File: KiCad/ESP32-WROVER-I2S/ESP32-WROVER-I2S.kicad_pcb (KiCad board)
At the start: 2 copper layers, 72 x 47 mm, 31 parts, among them J1 Ext_con, J2 Audio_Con, J3 USB_C_Receptacle_USB2.0_16P, Q1 BSS138, Q2 BSS138, SW1 FLASH, SW2 RESET, U1 ESP32-WROVER, U2 AMS1117-3.3, U3 CH340K

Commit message: ガーバー出力
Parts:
- removed C7: 1u, Capacitor_SMD:C_0603_1608Metric_Pad1.08x0.95mm_HandSolder
- removed C8: 0.1u, Capacitor_SMD:C_0603_1608Metric_Pad1.08x0.95mm_HandSolder
- removed Q1, Q2: BSS138, Package_TO_SOT_SMD:SOT-23
- removed R5, R6: 5.1k, Resistor_SMD:R_0603_1608Metric_Pad0.98x0.95mm_HandSolder
- removed SW1: FLASH, Button_Switch_SMD:SW_Push_SPST_NO_Alps_SKRK
- removed SW2: RESET, Button_Switch_SMD:SW_Push_SPST_NO_Alps_SKRK
- removed U3: CH340K, Package_SO:SSOP-10-1EP_3.9x4.9mm_P1mm_EP2.1x3.3mm
- added D3: D_Schottky, Diode_SMD:D_SOD-123, F.Cu at (157.0, 106.2)
- added J4: Downloader, Connector_PinSocket_2.54mm:PinSocket_1x06_P2.54mm_Vertical, F.Cu at (153.5, 86.4)
- J2: footprint Connector_PinHeader_2.54mm:PinHeader_1x03_P2.54mm_Vertical -> Connector_JST:JST_XH_B3B-XH-A_1x03_P2.50mm_Vertical
- J3: value USB_C_Receptacle_USB2.0_16P -> Power_Con; footprint Connector_USB:USB_C_Receptacle_XKB_U262-16XN-4BVC11 -> Connector_JST:JST_XH_B2B-XH-A_1x02_P2.50mm_Vertical
- moved J3 52.5 mm to (171.5, 111.8), turned to 0 degrees
- moved U2 48.8 mm to (162.6, 110.2), turned to -90 degrees
- moved D1 45.9 mm to (175.8, 107.3)
- moved F1 44.9 mm to (170.8, 107.0), turned to 180 degrees
- moved C1 44.3 mm to (160.6, 104.0), turned to 0 degrees
- moved R1 42.9 mm to (175.8, 105.5)
- moved J1 40.7 mm to (203.3, 74.7)
- moved J2 38.1 mm to (181.7, 90.8), turned to 90 degrees
- moved C2 38.0 mm to (164.4, 104.0), turned to 0 degrees
- moved C6 25.8 mm to (206.0, 109.9)
- moved A1 9.26 mm to (196.2, 98.9), turned to 90 degrees
- moved H2 9.00 mm to (210.0, 73.0)
- moved H4 9.00 mm to (210.0, 114.0)
- moved R3 7.57 mm to (181.5, 96.2), turned to 180 degrees
- moved R2 6.89 mm to (154.2, 82.1)
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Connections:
- C2 pad 1: +3.3V -> Net-(D3-A)
- F1 pad 1: Net-(F1-Pad1) -> Net-(J3-Pin_1)
- U2 pad 2: +3.3V -> Net-(D3-A)
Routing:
- net GND: track 278.0 -> 192.6 mm, vias 5 -> 7
- net +3.3V: track 131.0 -> 183.3 mm, vias 2 -> 1
- net /GPIO34: track 37.0 -> 81.3 mm, vias 1 -> 0
- net /DN: track 40.0 -> 0.00 mm
- net /DP: track 29.0 -> 0.00 mm
- net /GPIO13: track 10.8 -> 37.6 mm
- net /GPIO14: track 17.7 -> 43.2 mm
- net +5V: track 84.5 -> 59.5 mm
- net /EN: track 43.0 -> 18.6 mm, vias 2 -> 0
- net /GPIO12: track 14.5 -> 37.9 mm
- net /DTR: track 22.1 -> 0.00 mm, vias 2 -> 0
- net /GPIO33: track 23.9 -> 42.7 mm
- net /GPIO32: track 26.4 -> 44.2 mm
- net Net-(D3-A): track 0.00 -> 16.7 mm
- net /RTS: track 15.6 -> 0.00 mm, vias 2 -> 0
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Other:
- board size 72 x 47 mm -> 63 x 47 mm
- board text added: "3.3V"
- board text added: "3.3v"
- board text added: "5V GND"
- board text added: "Downloader"
- board text added: "EN"
- board text added: "ESP32-WROVER & I2S REV1 KUNI-NET 2025"
- board text added: "GPIO0"
- board text added: "ROUT GND LOUT"
- board text added: "RxD->TxD"
- board text added: "TxD->RxD"
- board text removed: "ESP32-WROVER & I2S BOARD REV1"
- board text removed: "FLASH"
- board text removed: "KUNI-NET 2025"
- board text removed: "RESET"

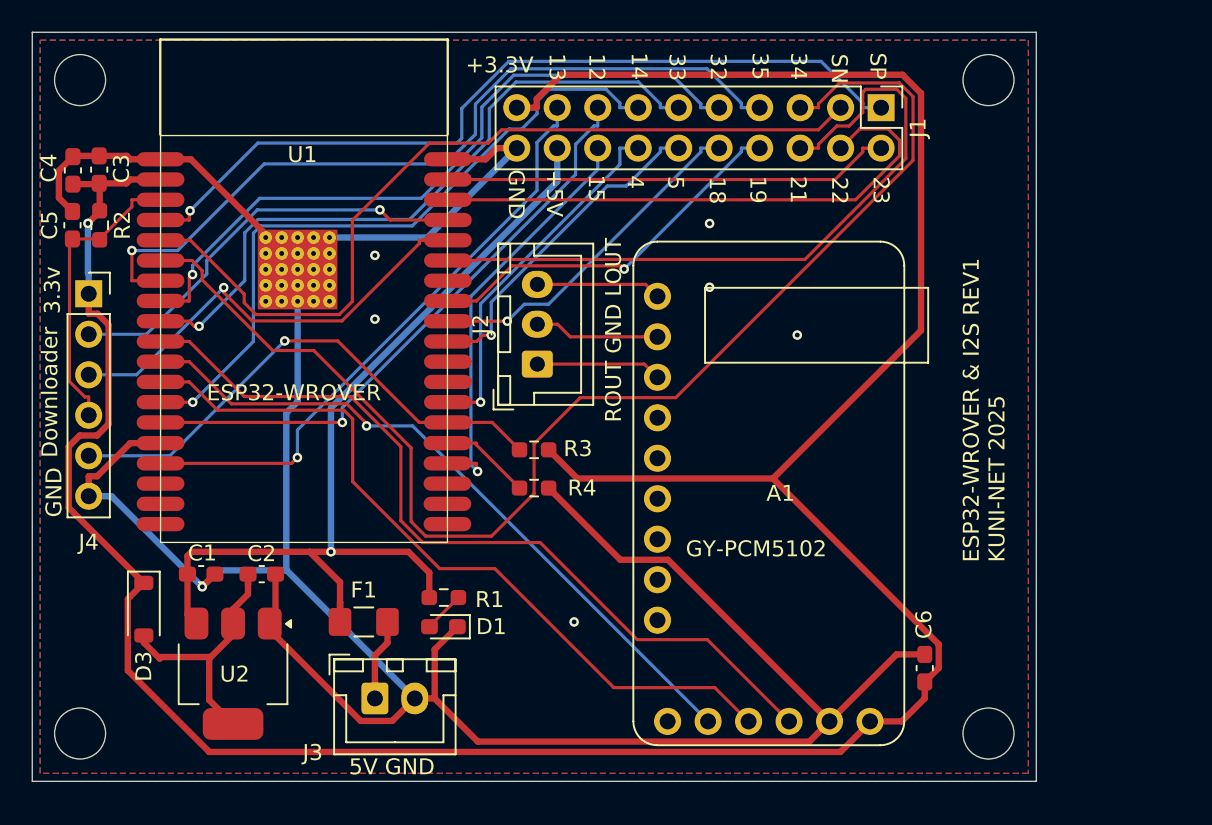
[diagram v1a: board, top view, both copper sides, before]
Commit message: 5v/3.3v切り替えジャンパ追加、電源LED変更、REV1.1ガーバー出力
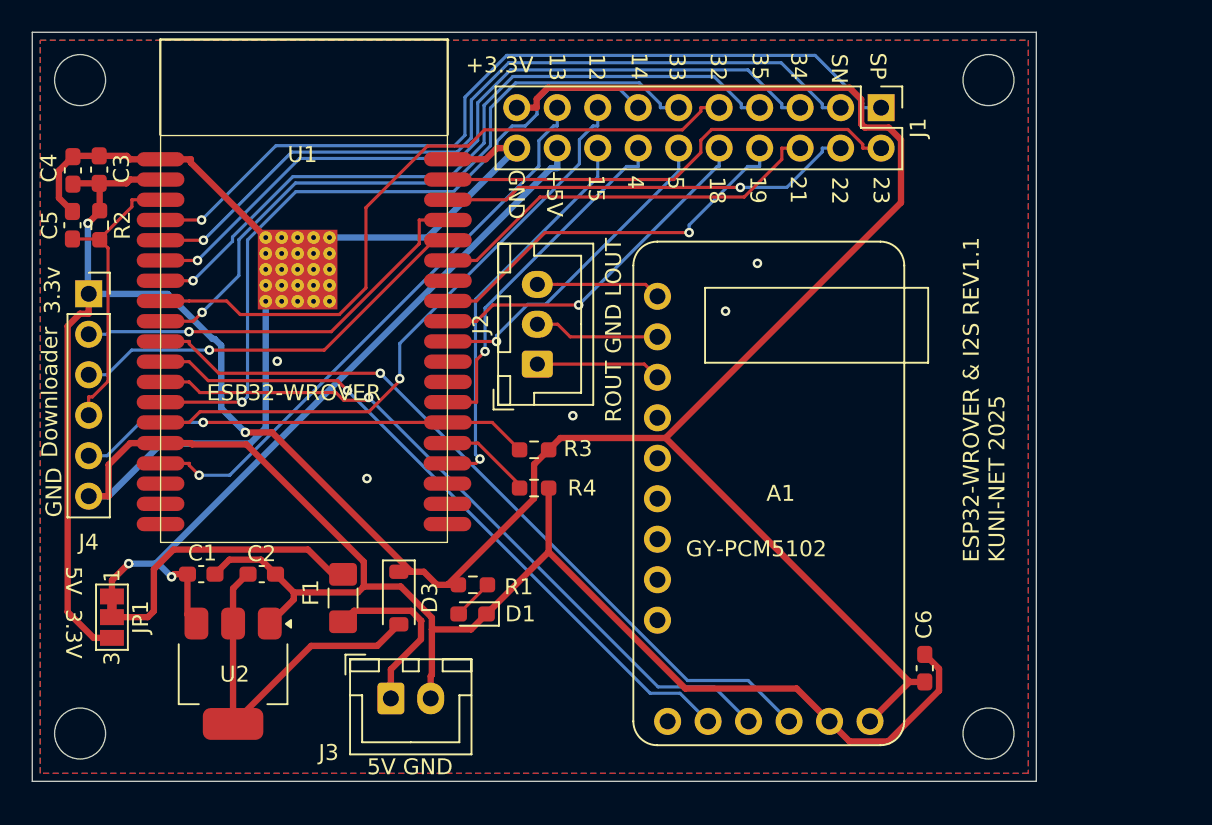
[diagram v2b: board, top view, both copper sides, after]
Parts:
- added JP1: V_JP, Jumper:SolderJumper-3_P1.3mm_Bridged12_Pad1.0x1.5mm_NumberLabels, F.Cu at (155.0, 106.7)
- moved D3 16.0 mm to (173.0, 105.5)
- moved R1 1.99 mm to (177.6, 104.7)
- moved D1 1.99 mm to (177.6, 106.5)
- moved F1 1.98 mm to (169.5, 105.5), turned to 90 degrees
- moved J3 1.00 mm to (172.5, 111.8)
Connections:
- F1 pad 2: +5V -> Net-(JP1-C)
- R1 pad 1: +5V -> +3.3V
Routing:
- net /GPIO34: track 81.3 -> 47.6 mm, vias 0 -> 1
- net /GPIO21: track 44.4 -> 25.4 mm
- net Net-(JP1-C): track 0.00 -> 18.4 mm
- net GND: track 192.6 -> 176.7 mm, vias 7 -> 5
- net +3.3V: track 183.3 -> 167.9 mm, vias 1 -> 2
- net +5V: track 59.5 -> 46.7 mm, vias 1 -> 2
- net /GPIO22: track 34.9 -> 26.1 mm, vias 0 -> 1
- net Net-(D3-A): track 16.7 -> 22.8 mm
- net Net-(J3-Pin_1): track 5.78 -> 11.6 mm
- net /GPIO35: track 50.1 -> 45.4 mm
- net /GPIO0: track 32.8 -> 28.6 mm
- net /SENSE_VN: track 53.3 -> 50.0 mm, vias 0 -> 1
- net Net-(A1-LCK): track 52.0 -> 49.4 mm, vias 0 -> 1
- net Net-(A1-DIN): track 48.0 -> 45.9 mm, vias 0 -> 1
- net /RxD0: track 28.1 -> 26.0 mm
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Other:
- board text added: "5V 3.3V"
- board text added: "ESP32-WROVER & I2S REV1.1 KUNI-NET 2025"
- board text removed: "ESP32-WROVER & I2S REV1 KUNI-NET 2025"
